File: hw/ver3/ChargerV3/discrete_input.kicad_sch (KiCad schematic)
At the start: 2 parts, among them U14 74HC595, U15 74HC595

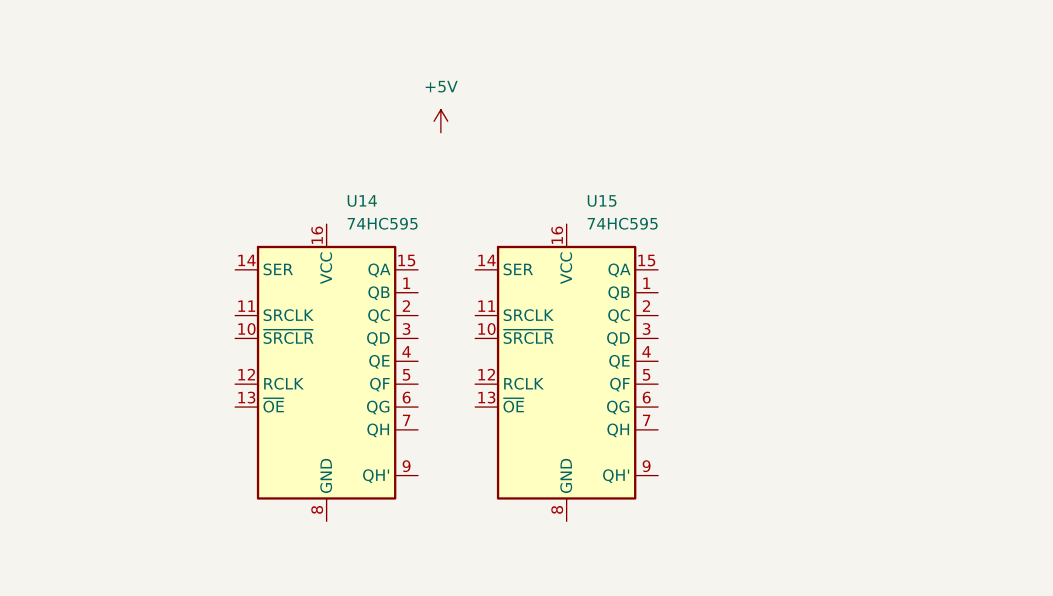
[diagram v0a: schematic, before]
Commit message: Split the design into four major components. Start working on system architecture.
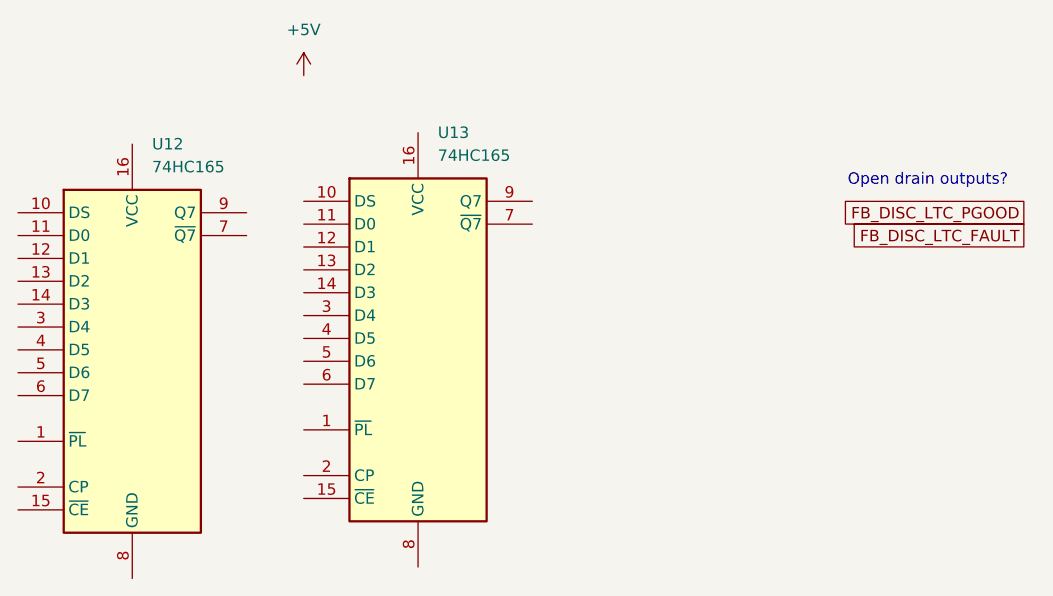
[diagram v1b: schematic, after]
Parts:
- removed U14, U15: 74HC595, symbol 74xx:74HC595
- added U12, U13: 74HC165, symbol 74xx:74HC165
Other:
- note added: "Open drain outputs?"
